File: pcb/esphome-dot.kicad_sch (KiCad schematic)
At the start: 18 parts, among them J1 Input, J2 Even, J3 Odd, J4 Output, J5 SPK1, J6 SPK2, U1 W25Q128JVSIQ, U2 ESP32-S3R8, Y1 40MHz

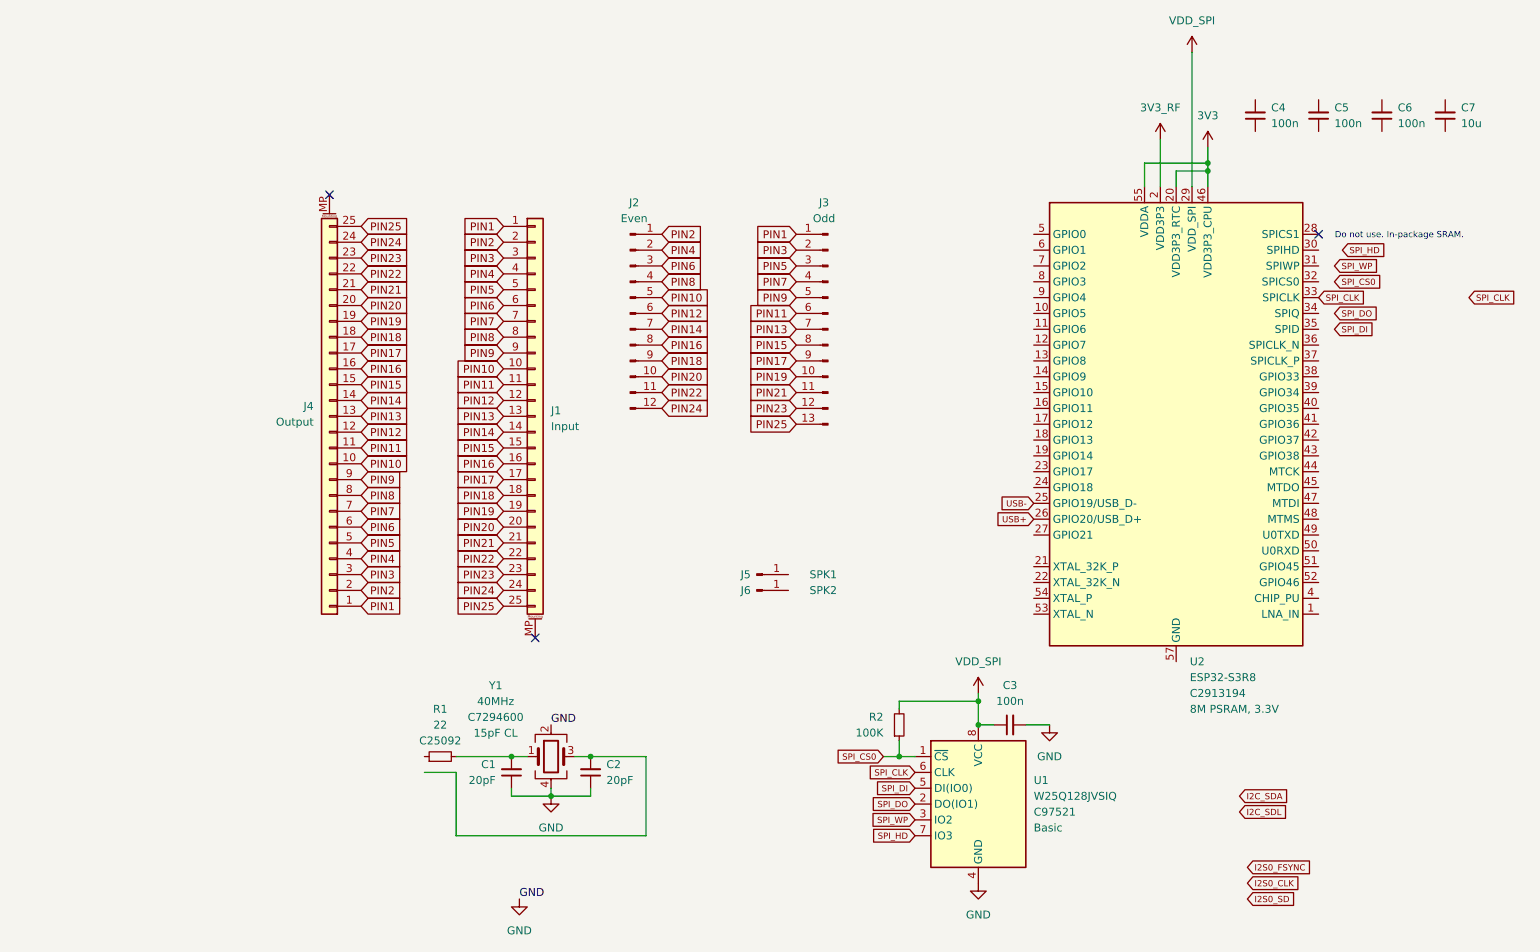
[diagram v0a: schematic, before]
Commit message: pcb-fitment-v2
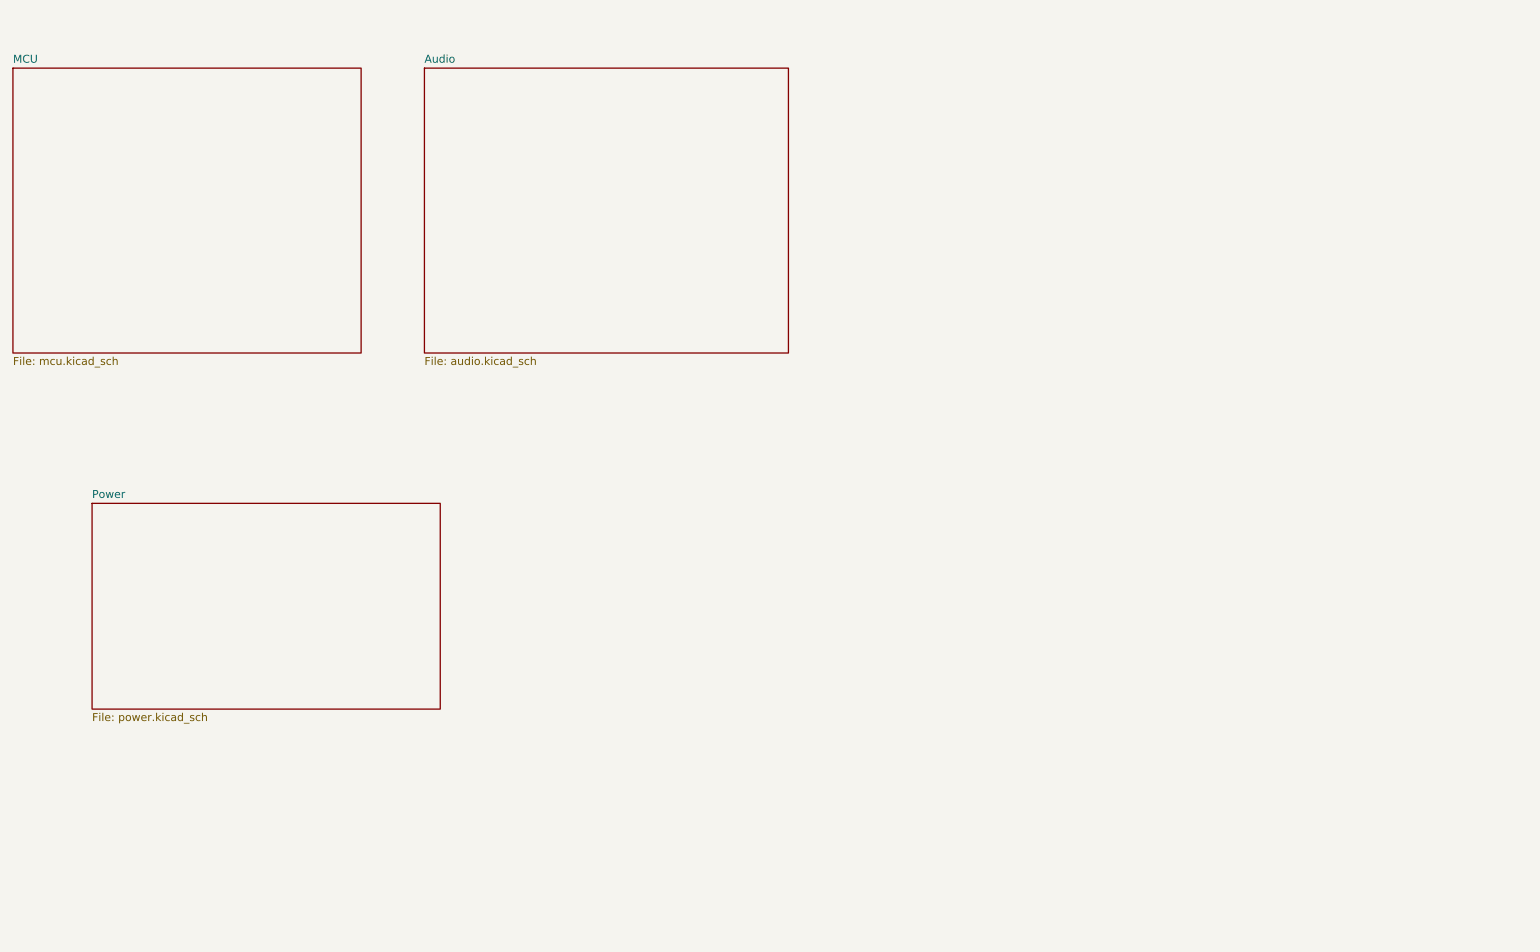
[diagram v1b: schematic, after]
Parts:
- removed C1, C2: 20pF, Capacitor_SMD:C_0402_1005Metric, symbol Device:C_Small
- removed C3, C4, C5, C6: 100n, symbol Device:C_Small
- removed C7: 10u, symbol Device:C_Small
- removed J1: Input, alexa:CONN_502598-2593_MOLEX, symbol Connector_Generic_MountingPin:Conn_01x25_MountingPin
- removed J2: Even, Connector_PinHeader_2.54mm:PinHeader_1x12_P2.54mm_Vertical, symbol Connector:Conn_01x12_Pin
- removed J3: Odd, Connector_PinHeader_2.54mm:PinHeader_1x13_P2.54mm_Vertical, symbol Connector:Conn_01x13_Pin
- removed J4: Output, alexa:CONN_502598-2593_MOLEX, symbol Connector_Generic_MountingPin:Conn_01x25_MountingPin
- removed J5: SPK1, alexa:SF2212, symbol Connector:Conn_01x01_Pin
- removed J6: SPK2, alexa:SF2212, symbol Connector:Conn_01x01_Pin
- removed R1: 22, Resistor_SMD:R_0402_1005Metric, symbol Device:R_Small
- removed R2: 100K, symbol Device:R_Small
- removed U1: W25Q128JVSIQ, Package_SO:SOIC-8_5.23x5.23mm_P1.27mm, symbol Memory_Flash:W25Q128JVS
- removed U2: ESP32-S3R8, Package_DFN_QFN:QFN-56-1EP_7x7mm_P0.4mm_EP4x4mm, symbol MCU_Espressif:ESP32-S3
- removed Y1: 40MHz, Crystal:Crystal_SMD_3225-4Pin_3.2x2.5mm, symbol Device:Crystal_GND24
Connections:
- no-connect marks 3 -> 0
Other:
- added sheet Audio (audio.kicad_sch)
- added sheet MCU (mcu.kicad_sch)
- added sheet Power (power.kicad_sch)
- note removed: "Do not use. In-package SRAM."
